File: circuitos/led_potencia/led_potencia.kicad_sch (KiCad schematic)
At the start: 45 parts, among them J1 Conn_01x02_Pin, J10 Conn_01x02_Pin, J11 Conn_01x02_Pin, J12 Conn_01x02_Pin, J13 Conn_01x02_Pin, J14 Conn_01x02_Pin, J15 Conn_01x02_Pin, J16 Conn_01x02_Pin, J2 Conn_01x02_Pin, J3 Conn_01x02_Pin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

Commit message: mejorando array
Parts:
- removed Q16, Q17, Q23: IRF4905, Package_TO_SOT_THT:TO-220-3_Vertical, symbol Transistor_FET:IRF4905
- removed Q19, Q20: PN2222A, Package_TO_SOT_THT:TO-92_Inline, symbol Transistor_BJT:PN2222A
- removed R10, R9: 10k, symbol Device:R
- added Q19, Q20, Q24: IRF4905, Package_TO_SOT_THT:TO-220-3_Vertical, symbol Transistor_FET:IRF4905
- added Q23, Q25: PN2222A, Package_TO_SOT_THT:TO-92_Inline, symbol Transistor_BJT:PN2222A
- added R13, R14: 10k, symbol Device:R
- R1, R2, R3, R4, R5, R6, R7, R8: value R -> 1k
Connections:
- net +12V: now also Q19.2 (D), Q20.2 (D), Q24.2 (D), R13.1, R14.1
- net GND: now also Q23.1 (E), Q25.1 (E)
- net at J14.2 (Pin_2): now also J10.2 (Pin_2), J2.2 (Pin_2), J6.2 (Pin_2), Q19.3 (S)
- net at J8.1 (Pin_1): now also J5.1 (Pin_1), J6.1 (Pin_1), J7.1 (Pin_1), Q3.2 (D)
- net at J12.2 (Pin_2), J16.2 (Pin_2), J8.2 (Pin_2): now also J4.2 (Pin_2), Q24.3 (S); no longer J1.2 (Pin_2)
- net at Q18.3 (S): now also J1.2 (Pin_2), J13.2 (Pin_2), J5.2 (Pin_2), J9.2 (Pin_2)
- net at R6.2: now also Q25.2 (B); no longer Q22.2 (B)
- net at J1.1 (Pin_1), J2.1 (Pin_1), J3.1 (Pin_1)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: now also Q4.2 (D); no longer Q3.2 (D)
- net at Q22.3 (C), R12.2: now also Q19.1 (G)
- net at R5.2: now also Q23.2 (B)
- net at J11.2 (Pin_2), J15.2 (Pin_2), J3.2 (Pin_2)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: now also Q20.3 (S)
- net at R1.2: now also Q22.2 (B)
- new net: Q20.1 (G), Q23.3 (C), R13.2
- new net: Q24.1 (G), Q25.3 (C), R14.2
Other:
- moved on the sheet: Q1, Q18, Q2, Q21, Q3, Q4, R11, R17, R18, R19, R20

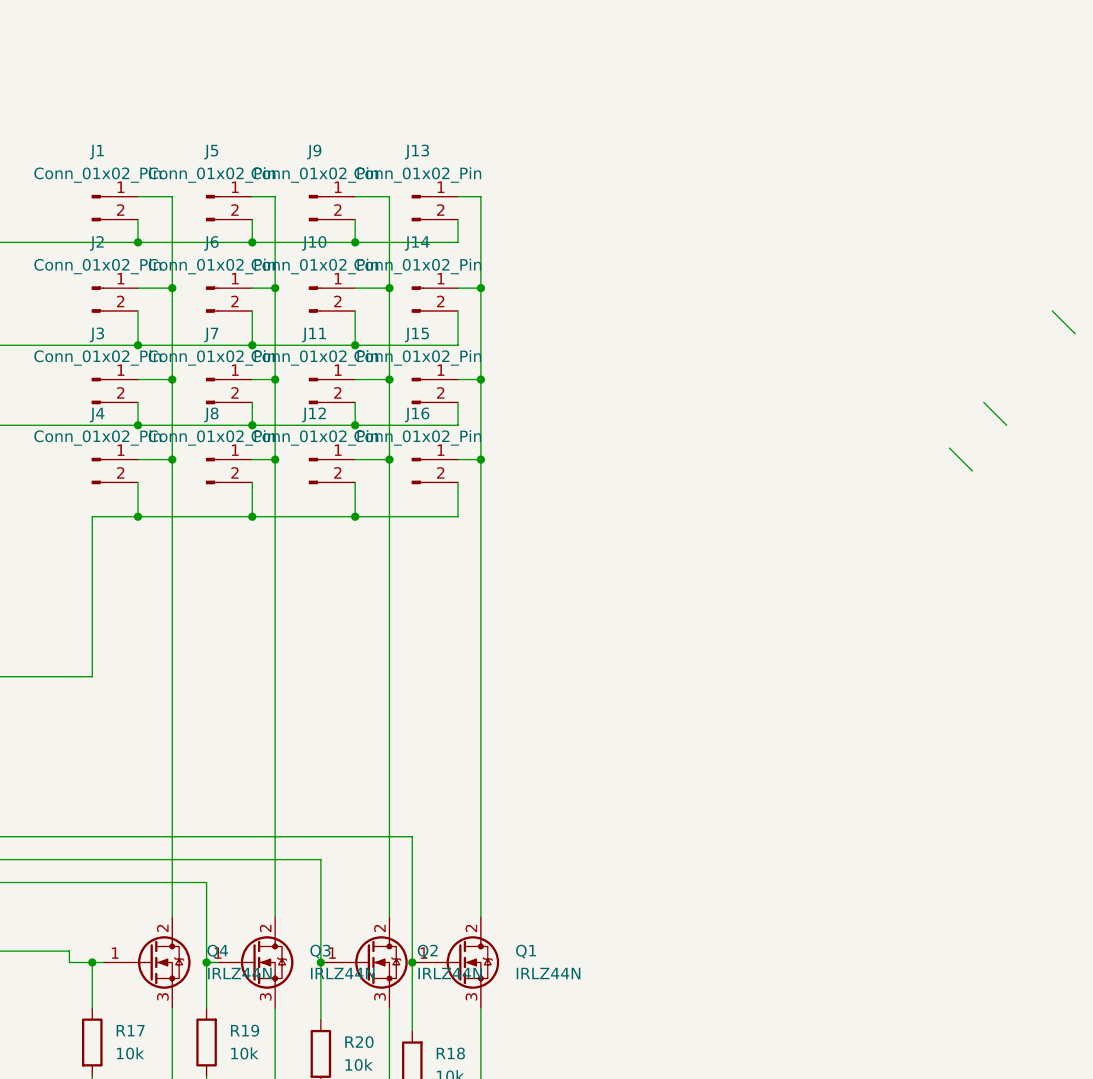
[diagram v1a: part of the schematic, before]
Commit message: logica funcionan pasando a pcb
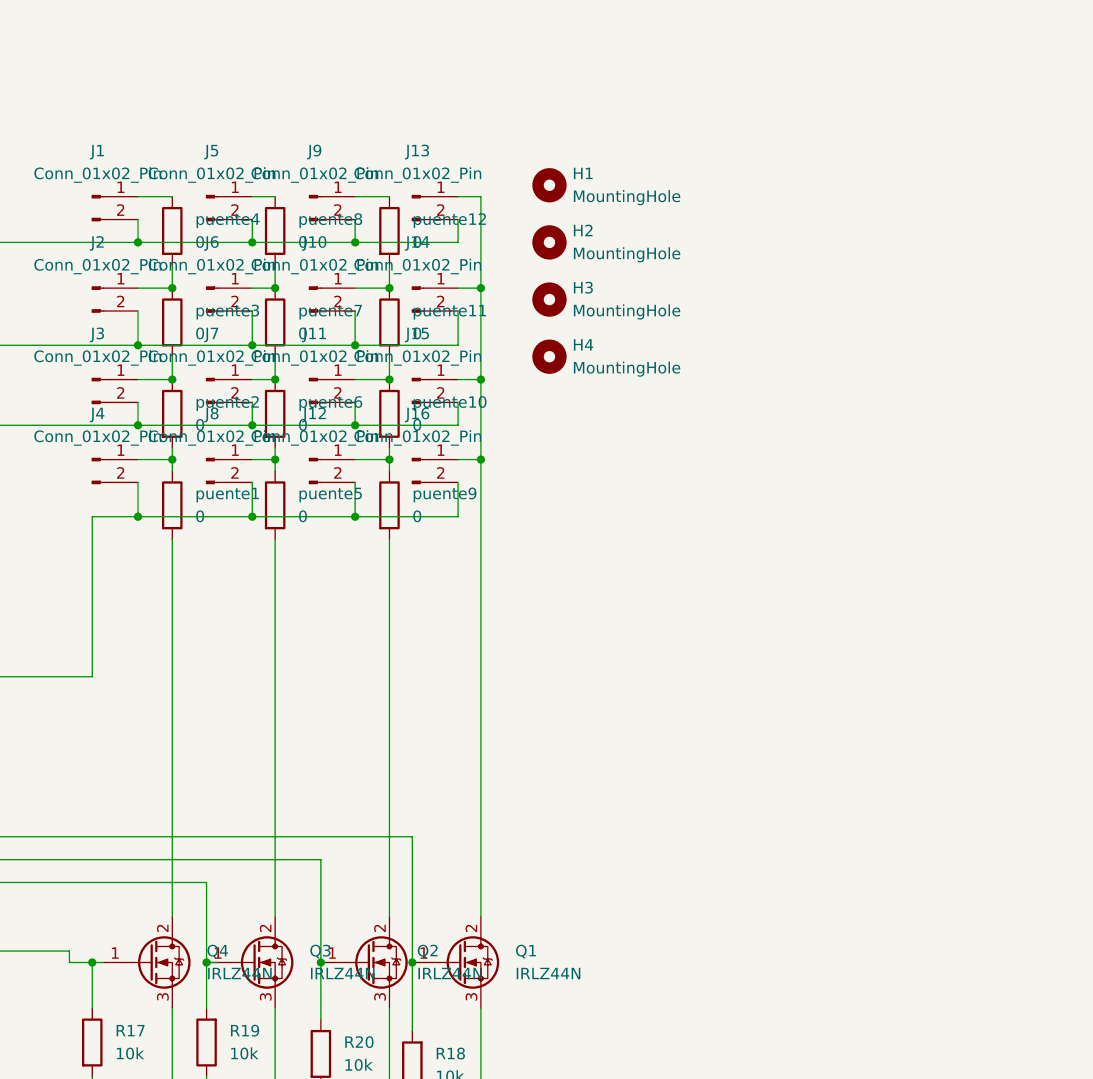
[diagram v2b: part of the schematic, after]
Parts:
- added H1, H2, H3, H4: MountingHole, MountingHole:MountingHole_2.2mm_M2_DIN965_Pad, symbol Mechanical:MountingHole
- added puente1, puente10, puente11, puente12, puente2, puente3, puente4, puente5, puente6, puente7, puente8, puente9: 0, Resistor_THT:R_Axial_DIN0309_L9.0mm_D3.2mm_P15.24mm_Horizontal, symbol Device:R
- J1, J10, J11, J12, J13, J14, J15, J16, J2, J3, J4, J5, J6, J7, J8, J9: footprint (none) -> Connector_Molex:Molex_KK-254_AE-6410-02A_1x02_P2.54mm_Vertical
- R1, R11, R12, R13, R14, R17, R18, R19, R2, R20, R3, R4, R5, R6, R7, R8: footprint (none) -> Resistor_THT:R_Axial_DIN0309_L9.0mm_D3.2mm_P12.70mm_Horizontal
- U1: footprint (none) -> Package_DIP:DIP-16_W7.62mm_Socket_LongPads
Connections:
- new net: J4.1 (Pin_1), puente1.1, puente2.2
- new net: J2.1 (Pin_1), puente3.1, puente4.2
- new net: J3.1 (Pin_1), puente2.1, puente3.2
- new net: J11.1 (Pin_1), puente10.1, puente11.2
- new net: J12.1 (Pin_1), puente10.2, puente9.1
- new net: J1.1 (Pin_1), puente4.1
- new net: J7.1 (Pin_1), puente6.1, puente7.2
- new net: J8.1 (Pin_1), puente5.1, puente6.2
- new net: J5.1 (Pin_1), puente8.1
- new net: J9.1 (Pin_1), puente12.1
- new net: Q4.2 (D), puente1.2
- new net: J6.1 (Pin_1), puente7.1, puente8.2
- new net: J10.1 (Pin_1), puente11.1, puente12.2
- new net: Q2.2 (D), puente9.2
- new net: Q3.2 (D), puente5.2

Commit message: sumando cambios
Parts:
- added J17, J18: Conn_01x02_Socket, Connector_Molex:Molex_KK-254_AE-6410-02A_1x02_P2.54mm_Vertical, symbol Connector:Conn_01x02_Socket
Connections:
- net +12V: now also J17.1 (Pin_1)
- net GND: now also J17.2 (Pin_2), J18.2 (Pin_2)
- net VCC: now also J18.1 (Pin_1)

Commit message: armando grilla PCB
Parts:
- puente1, puente10, puente11, puente12, puente2, puente3, puente4, puente5, puente6, puente7, puente8, puente9: footprint Resistor_THT:R_Axial_DIN0309_L9.0mm_D3.2mm_P15.24mm_Horizontal -> Resistor_THT:R_Axial_DIN0204_L3.6mm_D1.6mm_P5.08mm_Horizontal
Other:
- moved on the sheet: J17, J18
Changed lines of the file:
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@@
 	(paper "A4")
 	(junction
-		(at 44.45 140.97)
-		(diameter 0)
-		(color 0 0 0 0)
-	)
-	(junction
 		(at 215.9 67.31)
 		(diameter 0)
@@
 	)
 	(junction
-		(at 113.03 20.32)
-		(diameter 0)
-		(color 0 0 0 0)
-	)
-	(junction
 		(at 190.5 54.61)
 		(diameter 0)
@@
 	)
 	(junction
+		(at 52.07 140.97)
+		(diameter 0)
+		(color 0 0 0 0)
+	)
+	(junction
 		(at 201.93 63.5)
 		(diameter 0)
@@
 	(wire
 		(pts
-			(xy 29.21 35.56) (xy 29.21 140.97)
+			(xy 44.45 54.61) (xy 44.45 140.97)
 		)
 		(stroke
@@
 	(wire
 		(pts
-			(xy 29.21 140.97) (xy 44.45 140.97)
+			(xy 44.45 140.97) (xy 52.07 140.97)
 		)
 		(stroke
@@
 	(wire
 		(pts
+			(xy 113.03 24.13) (xy 113.03 29.21)
+		)
+		(stroke
+			(width 0)
+			(type default)
+		)
+	)
+	(wire
+		(pts
 			(xy 181.61 76.2) (xy 181.61 118.11)
 		)
@@
 	(wire
 		(pts
-			(xy 44.45 82.55) (xy 87.63 82.55)
+			(xy 52.07 82.55) (xy 87.63 82.55)
 		)
 		(stroke
@@
 	(wire
 		(pts
-			(xy 44.45 107.95) (xy 44.45 140.97)
+			(xy 52.07 107.95) (xy 52.07 140.97)
 		)
 		(stroke
@@
 	(wire
 		(pts
-			(xy 82.55 20.32) (xy 113.03 20.32)
+			(xy 44.45 29.21) (xy 113.03 29.21)
 		)
 		(stroke
@@
 	(wire
 		(pts
-			(xy 82.55 35.56) (xy 29.21 35.56)
-		)
-		(stroke
-			(width 0)
-			(type default)
-		)
-	)
-	(wire
-		(pts
 			(xy 123.19 36.83) (xy 120.65 36.83)
 		)
@@
 	(wire
 		(pts
-			(xy 44.45 140.97) (xy 87.63 140.97)
-		)
-		(stroke
-			(width 0)
-			(type default)
-		)
-	)
-	(wire
-		(pts
 			(xy 213.36 63.5) (xy 213.36 60.96)
 		)
@@
 	(wire
 		(pts
-			(xy 113.03 8.89) (xy 113.03 20.32)
-		)
-		(stroke
-			(width 0)
-			(type default)
-		)
-	)
-	(wire
-		(pts
 			(xy 128.27 99.06) (xy 125.73 99.06)
 		)
@@
 	(wire
 		(pts
-			(xy 113.03 20.32) (xy 113.03 29.21)
-		)
-		(stroke
-			(width 0)
-			(type default)
-		)
-	)
-	(wire
-		(pts
 			(xy 213.36 54.61) (xy 213.36 50.8)
 		)
@@
 	(wire
 		(pts
-			(xy 44.45 105.41) (xy 44.45 82.55)
+			(xy 52.07 105.41) (xy 52.07 82.55)
 		)
 		(stroke
@@
 	(wire
 		(pts
-			(xy 82.55 33.02) (xy 82.55 20.32)
+			(xy 44.45 52.07) (xy 44.45 29.21)
 		)
 		(stroke
@@
 	(wire
 		(pts
+			(xy 52.07 140.97) (xy 87.63 140.97)
+		)
+		(stroke
+			(width 0)
+			(type default)
+		)
+	)
+	(wire
+		(pts
 			(xy 129.54 99.06) (xy 128.27 99.06)
 		)
@@
 	(symbol
 		(lib_id "power:+12V")
-		(at 113.03 8.89 0)
+		(at 113.03 24.13 0)
 		(unit 1)
 		(body_style 1)
@@
 		(fields_autoplaced yes)
 		(property "Reference" "#PWR04"
-			(at 113.03 12.7 0)
+			(at 113.03 27.94 0)
 			(hide yes)
 			(show_name no)
@@
 		)
 		(property "Value" "+12V"
-			(at 113.03 3.81 0)
+			(at 113.03 19.05 0)
 			(show_name no)
 			(do_not_autoplace no)
@@
 		)
 		(property "Footprint" ""
-			(at 113.03 8.89 0)
+			(at 113.03 24.13 0)
 			(hide yes)
 			(show_name no)
@@
 		)
 		(property "Datasheet" ""
-			(at 113.03 8.89 0)
+			(at 113.03 24.13 0)
 			(hide yes)
 			(show_name no)
@@
 		)
 		(property "Description" "Power symbol creates a global label with name \"+12V\""
-			(at 113.03 8.89 0)
+			(at 113.03 24.13 0)
 			(hide yes)
 			(show_name no)
@@
 			)
 		)
-		(property "Footprint" "Resistor_THT:R_Axial_DIN0309_L9.0mm_D3.2mm_P15.24mm_Horizontal"
+		(property "Footprint" "Resistor_THT:R_Axial_DIN0204_L3.6mm_D1.6mm_P5.08mm_Horizontal"
 			(at 179.832 52.07 90)
 			(hide yes)
@@
 			)
 		)
-		(property "Footprint" "Resistor_THT:R_Axial_DIN0309_L9.0mm_D3.2mm_P15.24mm_Horizontal"
+		(property "Footprint" "Resistor_THT:R_Axial_DIN0204_L3.6mm_D1.6mm_P5.08mm_Horizontal"
 			(at 203.962 62.23 90)
 			(hide yes)
@@
 			)
 		)
-		(property "Footprint" "Resistor_THT:R_Axial_DIN0309_L9.0mm_D3.2mm_P15.24mm_Horizontal"
+		(property "Footprint" "Resistor_THT:R_Axial_DIN0204_L3.6mm_D1.6mm_P5.08mm_Horizontal"
 			(at 191.262 62.23 90)
 			(hide yes)
@@
 	(symbol
 		(lib_id "Connector:Conn_01x02_Socket")
-		(at 87.63 33.02 0)
+		(at 49.53 52.07 0)
 		(unit 1)
 		(body_style 1)
@@
 		(fields_autoplaced yes)
 		(property "Reference" "J17"
-			(at 88.9 33.0199 0)
+			(at 50.8 52.0699 0)
 			(show_name no)
 			(do_not_autoplace no)
@@
 		)
 		(property "Value" "Conn_01x02_Socket"
-			(at 88.9 35.5599 0)
+			(at 50.8 54.6099 0)
 			(show_name no)
 			(do_not_autoplace no)
@@
 		)
 		(property "Footprint" "Connector_Molex:Molex_KK-254_AE-6410-02A_1x02_P2.54mm_Vertical"
-			(at 87.63 33.02 0)
+			(at 49.53 52.07 0)
 			(hide yes)
 			(show_name no)
@@
 		)
 		(property "Datasheet" ""
-			(at 87.63 33.02 0)
+			(at 49.53 52.07 0)
 			(hide yes)
 			(show_name no)
@@
 		)
 		(property "Description" "Generic connector, single row, 01x02, script generated"
-			(at 87.63 33.02 0)
+			(at 49.53 52.07 0)
 			(hide yes)
 			(show_name no)
@@
 			)
 		)
-		(property "Footprint" "Resistor_THT:R_Axial_DIN0309_L9.0mm_D3.2mm_P15.24mm_Horizontal"
+		(property "Footprint" "Resistor_THT:R_Axial_DIN0204_L3.6mm_D1.6mm_P5.08mm_Horizontal"
 			(at 179.832 62.23 90)
 			(hide yes)
@@
 			)
 		)
-		(property "Footprint" "Resistor_THT:R_Axial_DIN0309_L9.0mm_D3.2mm_P15.24mm_Horizontal"
+		(property "Footprint" "Resistor_THT:R_Axial_DIN0204_L3.6mm_D1.6mm_P5.08mm_Horizontal"
 			(at 191.262 41.91 90)
 			(hide yes)
@@
 			)
 		)
-		(property "Footprint" "Resistor_THT:R_Axial_DIN0309_L9.0mm_D3.2mm_P15.24mm_Horizontal"
+		(property "Footprint" "Resistor_THT:R_Axial_DIN0204_L3.6mm_D1.6mm_P5.08mm_Horizontal"
 			(at 179.832 41.91 90)
 			(hide yes)
@@
 			)
 		)
-		(property "Footprint" "Resistor_THT:R_Axial_DIN0309_L9.0mm_D3.2mm_P15.24mm_Horizontal"
+		(property "Footprint" "Resistor_THT:R_Axial_DIN0204_L3.6mm_D1.6mm_P5.08mm_Horizontal"
 			(at 203.962 72.39 90)
 			(hide yes)
@@
 			)
 		)
-		(property "Footprint" "Resistor_THT:R_Axial_DIN0309_L9.0mm_D3.2mm_P15.24mm_Horizontal"
+		(property "Footprint" "Resistor_THT:R_Axial_DIN0204_L3.6mm_D1.6mm_P5.08mm_Horizontal"
 			(at 203.962 41.91 90)
 			(hide yes)
@@
 			)
 		)
-		(property "Footprint" "Resistor_THT:R_Axial_DIN0309_L9.0mm_D3.2mm_P15.24mm_Horizontal"
+		(property "Footprint" "Resistor_THT:R_Axial_DIN0204_L3.6mm_D1.6mm_P5.08mm_Horizontal"
 			(at 203.962 52.07 90)
 			(hide yes)
@@
 			)
 		)
-		(property "Footprint" "Resistor_THT:R_Axial_DIN0309_L9.0mm_D3.2mm_P15.24mm_Horizontal"
+		(property "Footprint" "Resistor_THT:R_Axial_DIN0204_L3.6mm_D1.6mm_P5.08mm_Horizontal"
 			(at 191.262 72.39 90)
 			(hide yes)
@@
 	(symbol
 		(lib_id "Connector:Conn_01x02_Socket")
-		(at 49.53 105.41 0)
+		(at 57.15 105.41 0)
 		(unit 1)
 		(body_style 1)
@@
 		(fields_autoplaced yes)
 		(property "Reference" "J18"
-			(at 50.8 105.4099 0)
+			(at 58.42 105.4099 0)
 			(show_name no)
 			(do_not_autoplace no)
@@
 		)
 		(property "Value" "Conn_01x02_Socket"
-			(at 50.8 107.9499 0)
+			(at 58.42 107.9499 0)
 			(show_name no)
 			(do_not_autoplace no)
@@
 		)
 		(property "Footprint" "Connector_Molex:Molex_KK-254_AE-6410-02A_1x02_P2.54mm_Vertical"
-			(at 49.53 105.41 0)
+			(at 57.15 105.41 0)
 			(hide yes)
 			(show_name no)
@@
 		)
 		(property "Datasheet" ""
-			(at 49.53 105.41 0)
+			(at 57.15 105.41 0)
 			(hide yes)
 			(show_name no)
@@
 		)
 		(property "Description" "Generic connector, single row, 01x02, script generated"
-			(at 49.53 105.41 0)
+			(at 57.15 105.41 0)
 			(hide yes)
 			(show_name no)
@@
 			)
 		)
-		(property "Footprint" "Resistor_THT:R_Axial_DIN0309_L9.0mm_D3.2mm_P15.24mm_Horizontal"
+		(property "Footprint" "Resistor_THT:R_Axial_DIN0204_L3.6mm_D1.6mm_P5.08mm_Horizontal"
 			(at 191.262 52.07 90)
 			(hide yes)
@@
 			)
 		)
-		(property "Footprint" "Resistor_THT:R_Axial_DIN0309_L9.0mm_D3.2mm_P15.24mm_Horizontal"
+		(property "Footprint" "Resistor_THT:R_Axial_DIN0204_L3.6mm_D1.6mm_P5.08mm_Horizontal"
 			(at 179.832 72.39 90)
 			(hide yes)

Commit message: circuito pre finalizado, retestear en proto e imprimir
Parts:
- removed J18: Conn_01x02_Socket, Connector_Molex:Molex_KK-254_AE-6410-02A_1x02_P2.54mm_Vertical, symbol Connector:Conn_01x02_Socket
- added J19: Conn_01x02_OE_GND, Connector_Molex:Molex_KK-254_AE-6410-02A_1x02_P2.54mm_Vertical, symbol Connector:Conn_01x02_Pin
- added J20: Conn_01x05_Pin, Connector_Molex:Molex_KK-254_AE-6410-05A_1x05_P2.54mm_Vertical, symbol Connector:Conn_01x05_Pin
- added Puente_GND1: 0, Resistor_THT:R_Axial_DIN0204_L3.6mm_D1.6mm_P7.62mm_Horizontal, symbol Device:R
- R1, R11, R12, R13, R14, R17, R18, R19, R2, R20, R3, R4, R5, R6, R7, R8: footprint Resistor_THT:R_Axial_DIN0309_L9.0mm_D3.2mm_P12.70mm_Horizontal -> Resistor_THT:R_Axial_DIN0204_L3.6mm_D1.6mm_P7.62mm_Horizontal
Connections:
- net GND: now also J19.1 (Pin_1), Puente_GND1.1
- net VCC: now also U1.10 (~{SRCLR}), J20.5 (Pin_5)
- net at R8.1: now also U1.5 (QF); no longer U1.6 (QG)
- net at U1.11 (SRCLK): now also J20.2 (Pin_2)
- net at U1.12 (RCLK): now also J20.3 (Pin_3)
- net at U1.13 (~{OE}): now also J19.2 (Pin_2)
- net at U1.14 (SER): now also J20.4 (Pin_4)
- net at U1.4 (QE): now also R4.1; no longer R3.1
- net at R7.1: now also U1.6 (QG); no longer U1.5 (QF)
- net at U1.7 (QH): now also R3.1; no longer R4.1
- new net: J20.1 (Pin_1), Puente_GND1.2
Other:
- note added: "molex 1 GND 2 SRCLK (clock) 3 RCLK( Latch) 4 SER (Serial) 5 VCC"
- moved on the sheet: R3, R4, R7, R8

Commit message: in out añadidos
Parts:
- added J21: Conn_01x05_OUT, Connector_Molex:Molex_KK-254_AE-6410-05A_1x05_P2.54mm_Vertical, symbol Connector:Conn_01x05_Pin
- added Puente_OE1: 0, Resistor_THT:R_Axial_DIN0204_L3.6mm_D1.6mm_P5.08mm_Horizontal, symbol Device:R
- J20: value Conn_01x05_Pin -> Conn_01x05_IN
- Puente_GND1: footprint Resistor_THT:R_Axial_DIN0204_L3.6mm_D1.6mm_P7.62mm_Horizontal -> Resistor_THT:R_Axial_DIN0207_L6.3mm_D2.5mm_P10.16mm_Horizontal
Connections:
- net VCC: now also J21.5 (Pin_5)
- net at J19.2 (Pin_2): now also Puente_OE1.1; no longer U1.13 (~{OE})
- net at J20.2 (Pin_2): now also U1.12 (RCLK), J21.2 (Pin_2); no longer U1.11 (SRCLK)
- net at J20.3 (Pin_3): now also U1.11 (SRCLK), J21.3 (Pin_3); no longer U1.12 (RCLK)
- net at U1.9 (QH'): now also J21.4 (Pin_4)
- net at J20.1 (Pin_1), Puente_GND1.2: now also J21.1 (Pin_1)
- new net: Puente_OE1.2, U1.13 (~{OE})
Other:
- moved on the sheet: J19
